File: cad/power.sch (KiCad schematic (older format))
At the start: 29 parts, among them SW1 SW_PUSH, U3 TPS73001, U4 TPS73001

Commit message: added more footprint stuff
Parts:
- D2: footprint (none) -> hlib:SOD-323
- R10, R11, R12, R13, R14, R15, R16, R17, R18, R19, R8, R9: footprint (none) -> Resistors_SMD:R_0402
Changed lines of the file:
@@
 LIBS:valves
 LIBS:misc
-LIBS:MPU-9250
-LIBS:p8x32a-lqfp
-LIBS:cc2541
 LIBS:device
 LIBS:smartercopter-cache
@@
 F 0 "R14" V 5630 3200 50  0000 C CNN
 F 1 "0" V 5550 3200 50  0000 C CNN
-F 2 "" H 5550 3200 60  0001 C CNN
+F 2 "Resistors_SMD:R_0402" H 5550 3200 60  0001 C CNN
 F 3 "" H 5550 3200 60  0000 C CNN
 F 4 "RC1005J000CS" V 5550 3200 60  0001 C CNN "MPN"
@@
 F 0 "R16" V 6280 2650 50  0000 C CNN
 F 1 "39k" V 6200 2650 50  0000 C CNN
-F 2 "" H 6200 2650 60  0001 C CNN
+F 2 "Resistors_SMD:R_0402" H 6200 2650 60  0001 C CNN
 F 3 "" H 6200 2650 60  0000 C CNN
 F 4 "RC1005J393CS" V 6200 2650 60  0001 C CNN "MPN"
@@
 F 0 "R17" V 6280 3250 50  0000 C CNN
 F 1 "30k" V 6200 3250 50  0000 C CNN
-F 2 "" H 6200 3250 60  0001 C CNN
+F 2 "Resistors_SMD:R_0402" H 6200 3250 60  0001 C CNN
 F 3 "" H 6200 3250 60  0000 C CNN
 F 4 "RC1005J303CS" V 6200 3250 60  0001 C CNN "MPN"
@@
 F 0 "R15" V 5630 4750 50  0000 C CNN
 F 1 "0" V 5550 4750 50  0000 C CNN
-F 2 "" H 5550 4750 60  0001 C CNN
+F 2 "Resistors_SMD:R_0402" H 5550 4750 60  0001 C CNN
 F 3 "" H 5550 4750 60  0000 C CNN
 	1    5550 4750
@@
 F 0 "R18" V 6280 4200 50  0000 C CNN
 F 1 "39k" V 6200 4200 50  0000 C CNN
-F 2 "" H 6200 4200 60  0001 C CNN
+F 2 "Resistors_SMD:R_0402" H 6200 4200 60  0001 C CNN
 F 3 "" H 6200 4200 60  0000 C CNN
 	1    6200 4200
@@
 F 0 "R19" V 6280 4800 50  0000 C CNN
 F 1 "30k" V 6200 4800 50  0000 C CNN
-F 2 "" H 6200 4800 60  0001 C CNN
+F 2 "Resistors_SMD:R_0402" H 6200 4800 60  0001 C CNN
 F 3 "" H 6200 4800 60  0000 C CNN
 	1    6200 4800
@@
 F 0 "R11" V 3630 3950 50  0000 C CNN
 F 1 "10" V 3550 3950 50  0000 C CNN
-F 2 "" H 3550 3950 60  0001 C CNN
+F 2 "Resistors_SMD:R_0402" H 3550 3950 60  0001 C CNN
 F 3 "" H 3550 3950 60  0000 C CNN
 F 4 "MCR01MRTF10R0" V 3550 3950 60  0001 C CNN "MPN"
@@
 F 0 "R10" V 2930 6500 50  0000 C CNN
 F 1 "100k" V 2850 6500 50  0000 C CNN
-F 2 "" H 2850 6500 60  0001 C CNN
+F 2 "Resistors_SMD:R_0402" H 2850 6500 60  0001 C CNN
 F 3 "" H 2850 6500 60  0000 C CNN
 F 4 "MCR01MRTF1003" V 2850 6500 60  0001 C CNN "MPN"
@@
 F 0 "D2" H 2150 7150 50  0000 C CNN
 F 1 "2.7v" H 2150 6950 40  0000 C CNN
-F 2 "" H 2150 7050 60  0001 C CNN
+F 2 "hlib:SOD-323" H 2150 7050 60  0001 C CNN
 F 3 "" H 2150 7050 60  0000 C CNN
 F 4 "MM3Z2V7T1G" H 2150 7050 60  0001 C CNN "MPN"
@@
 F 0 "R8" V 2230 6500 50  0000 C CNN
 F 1 "2k2" V 2150 6500 50  0000 C CNN
-F 2 "" H 2150 6500 60  0001 C CNN
+F 2 "Resistors_SMD:R_0402" H 2150 6500 60  0001 C CNN
 F 3 "" H 2150 6500 60  0000 C CNN
 F 4 "RMCF0402JT2K20" V 2150 6500 60  0001 C CNN "MPN"
@@
 F 0 "R9" V 2530 7050 50  0000 C CNN
 F 1 "20k" V 2450 7050 50  0000 C CNN
-F 2 "" H 2450 7050 60  0001 C CNN
+F 2 "Resistors_SMD:R_0402" H 2450 7050 60  0001 C CNN
 F 3 "" H 2450 7050 60  0000 C CNN
 F 4 "MCR01MRTF2002" V 2450 7050 60  0001 C CNN "MPN"
@@
 F 0 "R13" V 5380 6850 50  0000 C CNN
 F 1 "62k" V 5300 6850 50  0000 C CNN
-F 2 "" H 5300 6850 60  0001 C CNN
+F 2 "Resistors_SMD:R_0402" H 5300 6850 60  0001 C CNN
 F 3 "" H 5300 6850 60  0000 C CNN
 F 4 "MCR01MRTJ623" V 5300 6850 60  0001 C CNN "MPN"
@@
 F 0 "R12" V 5380 6250 50  0000 C CNN
 F 1 "36k" V 5300 6250 50  0000 C CNN
-F 2 "" H 5300 6250 60  0001 C CNN
+F 2 "Resistors_SMD:R_0402" H 5300 6250 60  0001 C CNN
 F 3 "" H 5300 6250 60  0000 C CNN
 F 4 "MCR01MRTF3602" V 5300 6250 60  0001 C CNN "MPN"

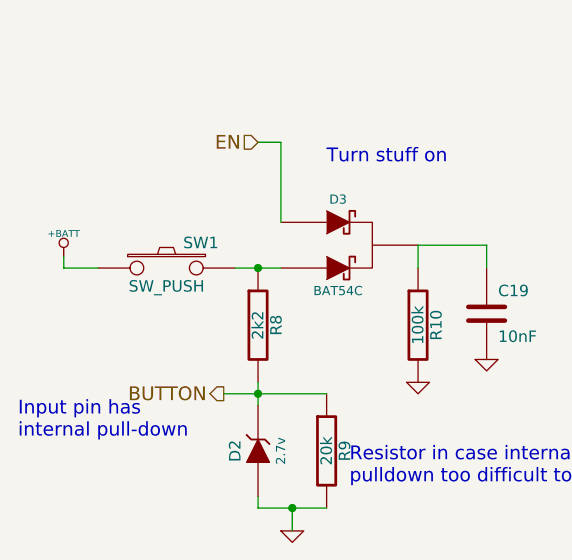
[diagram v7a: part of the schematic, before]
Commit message: bunch more footprints assigned
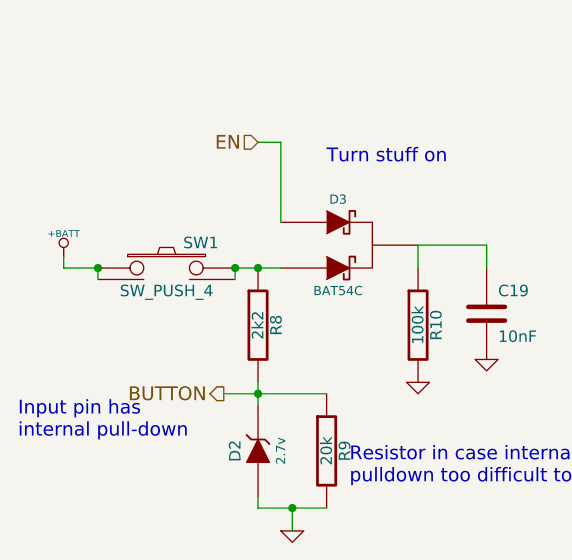
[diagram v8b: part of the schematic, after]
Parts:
- removed SW1: SW_PUSH, symbol SW_PUSH
- added SW1: SW_PUSH_4, hlib:PTS840GMSMTRLFS, symbol SW_PUSH_4
- U3, U4: footprint (none) -> SMD_Packages:SOT-23-6
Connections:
- net +BATT: now also SW1.1, SW1.2
- net at D3.2, R8.1: now also SW1.3, SW1.4
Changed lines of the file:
@@
-$EndComp
-$Comp
-L SW_PUSH SW1
-U 1 1 548F8D37
-P 1750 6250
-F 0 "SW1" H 1900 6360 50  0000 C CNN
-F 1 "SW_PUSH" H 1750 6170 50  0000 C CNN
-F 2 "" H 1750 6250 60  0001 C CNN
-F 3 "" H 1750 6250 60  0000 C CNN
-F 4 "PTS840 GM SMTR LFS" H 1750 6250 60  0001 C CNN "MPN"
-	1    1750 6250
-	1    0    0    -1
 $EndComp
 $Comp
@@
 F 0 "U3" H 5200 2750 60  0000 C CNN
 F 1 "TPS73001" H 5500 2250 60  0000 C CNN
-F 2 "" H 5250 2500 60  0001 C CNN
+F 2 "SMD_Packages:SOT-23-6" H 5250 2500 60  0001 C CNN
 F 3 "" H 5250 2500 60  0000 C CNN
 F 4 "TPS73001DBVR" H 5250 2500 60  0001 C CNN "MPN"
@@
 F 0 "U4" H 5200 4300 60  0000 C CNN
 F 1 "TPS73001" H 5500 3800 60  0000 C CNN
-F 2 "" H 5250 4050 60  0001 C CNN
+F 2 "SMD_Packages:SOT-23-6" H 5250 4050 60  0001 C CNN
 F 3 "" H 5250 4050 60  0000 C CNN
 	1    5250 4050
@@
 Text Notes 2450 5800 0    60   ~ 0
 Turn stuff on
+$Comp
+L SW_PUSH_4 SW1
+U 1 1 5497A571
+P 1750 6250
+F 0 "SW1" H 1900 6360 50  0000 C CNN
+F 1 "SW_PUSH_4" H 1750 6150 50  0000 C CNN
+F 2 "hlib:PTS840GMSMTRLFS" H 1750 6250 60  0001 C CNN
+F 3 "" H 1750 6250 60  0000 C CNN
+F 4 "PTS840 GM SMTR LFS" H 1750 6250 60  0001 C CNN "MPN"
+	1    1750 6250
+	1    0    0    -1
+$EndComp
+Wire Wire Line
+	2050 6300 2050 6250
+Connection ~ 2050 6250
+Wire Wire Line
+	1450 6250 1450 6300
+Connection ~ 1450 6250
 $EndSCHEMATC
